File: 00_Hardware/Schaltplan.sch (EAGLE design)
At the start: 108 parts, among them IC1 ATMEGA328P-AN, IC2 DS1307, J1 DCJ0202, Q1 16MHz, Q2 32.768 kHz

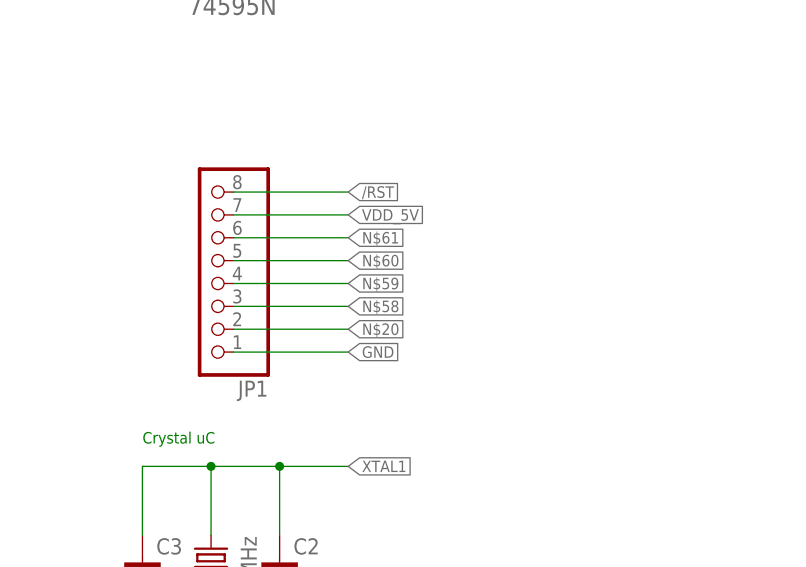
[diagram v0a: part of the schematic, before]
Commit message: Added missing spi connections in schematic
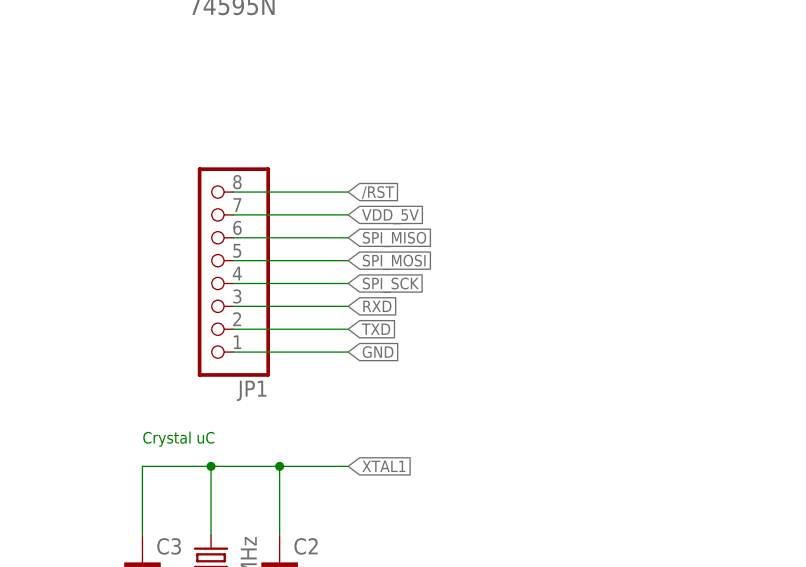
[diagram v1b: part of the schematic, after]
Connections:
- removed net N$20: JP1.2
- removed net N$58: JP1.3
- removed net N$59: JP1.4
- removed net N$60: JP1.5
- removed net N$61: JP1.6
- net RXD: now also JP1.3
- net SPI_MISO: now also JP1.6
- net SPI_MOSI: now also JP1.5
- net SPI_SCK: now also JP1.4
- net TXD: now also JP1.2
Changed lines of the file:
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@@
 <label x="15.24" y="25.4" size="1.27" layer="95" rot="R180" xref="yes"/>
+</segment>
+<segment>
+<pinref part="JP1" gate="A" pin="3"/>
+<wire x1="299.72" y1="134.62" x2="312.42" y2="134.62" width="0.1524" layer="91"/>
+<label x="312.42" y="134.62" size="1.27" layer="95" xref="yes"/>
 </segment>
 </net>
@@
 <wire x1="25.4" y1="27.94" x2="15.24" y2="27.94" width="0.1524" layer="91"/>
 <label x="15.24" y="27.94" size="1.27" layer="95" rot="R180" xref="yes"/>
+</segment>
+<segment>
+<pinref part="JP1" gate="A" pin="2"/>
+<wire x1="299.72" y1="132.08" x2="312.42" y2="132.08" width="0.1524" layer="91"/>
+<label x="312.42" y="132.08" size="1.27" layer="95" xref="yes"/>
 </segment>
 </net>
@@
 <label x="106.68" y="60.96" size="1.27" layer="95" xref="yes"/>
 </segment>
+<segment>
+<pinref part="JP1" gate="A" pin="4"/>
+<wire x1="299.72" y1="137.16" x2="312.42" y2="137.16" width="0.1524" layer="91"/>
+<label x="312.42" y="137.16" size="1.27" layer="95" xref="yes"/>
+</segment>
 </net>
 <net name="SPI_MISO" class="0">
@@
 <label x="106.68" y="58.42" size="1.27" layer="95" xref="yes"/>
 </segment>
+<segment>
+<pinref part="JP1" gate="A" pin="6"/>
+<wire x1="299.72" y1="142.24" x2="312.42" y2="142.24" width="0.1524" layer="91"/>
+<label x="312.42" y="142.24" size="1.27" layer="95" xref="yes"/>
+</segment>
 </net>
 <net name="SPI_MOSI" class="0">
@@
 <wire x1="96.52" y1="55.88" x2="106.68" y2="55.88" width="0.1524" layer="91"/>
 <label x="106.68" y="55.88" size="1.27" layer="95" xref="yes"/>
+</segment>
+<segment>
+<pinref part="JP1" gate="A" pin="5"/>
+<wire x1="299.72" y1="139.7" x2="312.42" y2="139.7" width="0.1524" layer="91"/>
+<label x="312.42" y="139.7" size="1.27" layer="95" xref="yes"/>
 </segment>
 </net>
@@
 </segment>
 </net>
-<net name="N$20" class="0">
-<segment>
-<pinref part="JP1" gate="A" pin="2"/>
-<wire x1="299.72" y1="132.08" x2="312.42" y2="132.08" width="0.1524" layer="91"/>
-<label x="312.42" y="132.08" size="1.27" layer="95" xref="yes"/>
-</segment>
-</net>
-<net name="N$58" class="0">
-<segment>
-<pinref part="JP1" gate="A" pin="3"/>
-<wire x1="299.72" y1="134.62" x2="312.42" y2="134.62" width="0.1524" layer="91"/>
-<label x="312.42" y="134.62" size="1.27" layer="95" xref="yes"/>
-</segment>
-</net>
-<net name="N$59" class="0">
-<segment>
-<pinref part="JP1" gate="A" pin="4"/>
-<wire x1="299.72" y1="137.16" x2="312.42" y2="137.16" width="0.1524" layer="91"/>
-<label x="312.42" y="137.16" size="1.27" layer="95" xref="yes"/>
-</segment>
-</net>
-<net name="N$60" class="0">
-<segment>
-<pinref part="JP1" gate="A" pin="5"/>
-<wire x1="299.72" y1="139.7" x2="312.42" y2="139.7" width="0.1524" layer="91"/>
-<label x="312.42" y="139.7" size="1.27" layer="95" xref="yes"/>
-</segment>
-</net>
-<net name="N$61" class="0">
-<segment>
-<pinref part="JP1" gate="A" pin="6"/>
-<wire x1="299.72" y1="142.24" x2="312.42" y2="142.24" width="0.1524" layer="91"/>
-<label x="312.42" y="142.24" size="1.27" layer="95" xref="yes"/>
-</segment>
-</net>

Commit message: Transfer files to Linux. Simple save
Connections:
- net BTN_ADD: now also IC1G$1.PD4(T0/XCK/PCINT20)
- net BTN_SET: no longer IC1G$1.PD4(T0/XCK/PCINT20)
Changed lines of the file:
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@@
 <setting verticaltext="up"/>
 </settings>
-<grid distance="0.1" unitdist="inch" unit="mm" style="lines" multiple="1" display="no" altdistance="0.01" altunitdist="inch" altunit="mm"/>
+<grid distance="0.1" unitdist="inch" unit="inch" style="lines" multiple="1" display="no" altdistance="0.01" altunitdist="inch" altunit="inch"/>
 <layers>
 <layer number="1" name="Top" color="4" fill="1" visible="no" active="no"/>
@@
 <junction x="269.24" y="27.94"/>
 </segment>
+<segment>
+<pinref part="IC1" gate="G$1" pin="PD4(T0/XCK/PCINT20)"/>
+<wire x1="25.4" y1="35.56" x2="15.24" y2="35.56" width="0.1524" layer="91"/>
+<label x="15.24" y="35.56" size="1.27" layer="95" rot="R180" xref="yes"/>
+</segment>
 </net>
 <net name="N$47" class="0">
@@
 </segment>
 <segment>
-<pinref part="IC1" gate="G$1" pin="PD4(T0/XCK/PCINT20)"/>
-<wire x1="25.4" y1="35.56" x2="15.24" y2="35.56" width="0.1524" layer="91"/>
-<label x="15.24" y="35.56" size="1.27" layer="95" rot="R180" xref="yes"/>
-</segment>
-<segment>
